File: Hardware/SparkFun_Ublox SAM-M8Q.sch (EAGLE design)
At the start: 34 parts, among them J13 Qwiic Right Angle, J4 Qwiic Right Angle, U2 UBLOX_SAM_M8Q-0-10

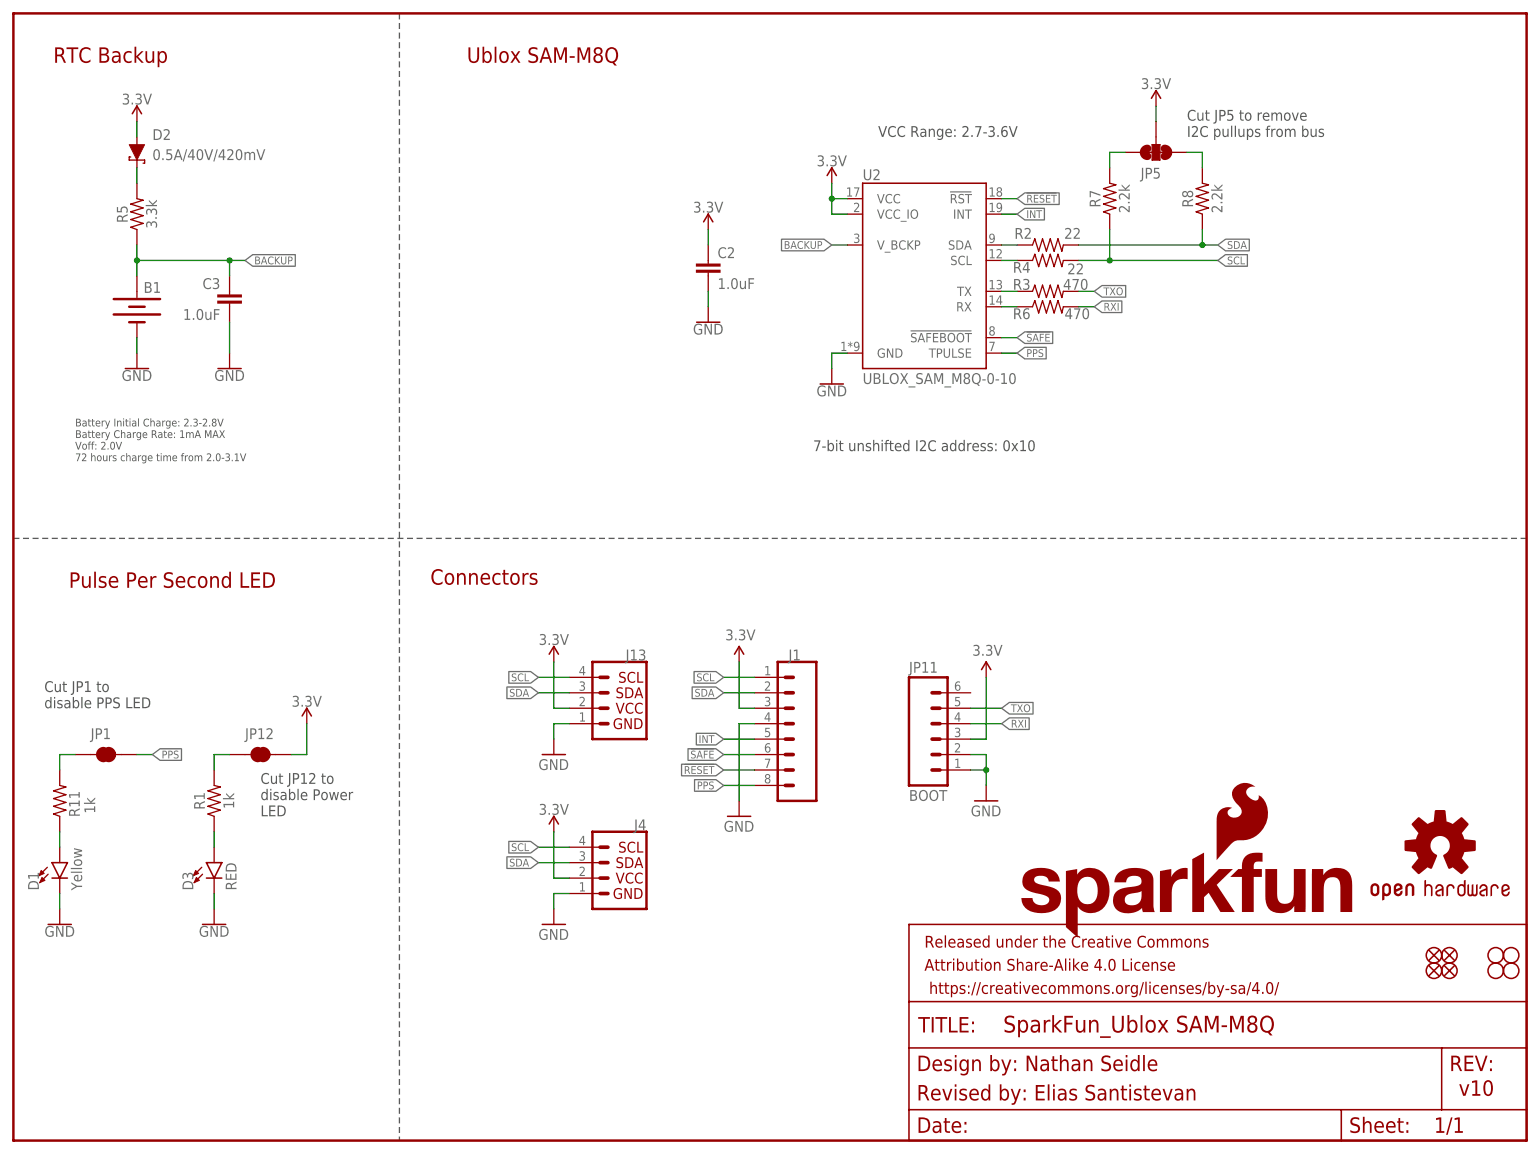
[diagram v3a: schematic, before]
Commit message: Changes JP12 to JP2, fixes SDA trace, adds silk on top
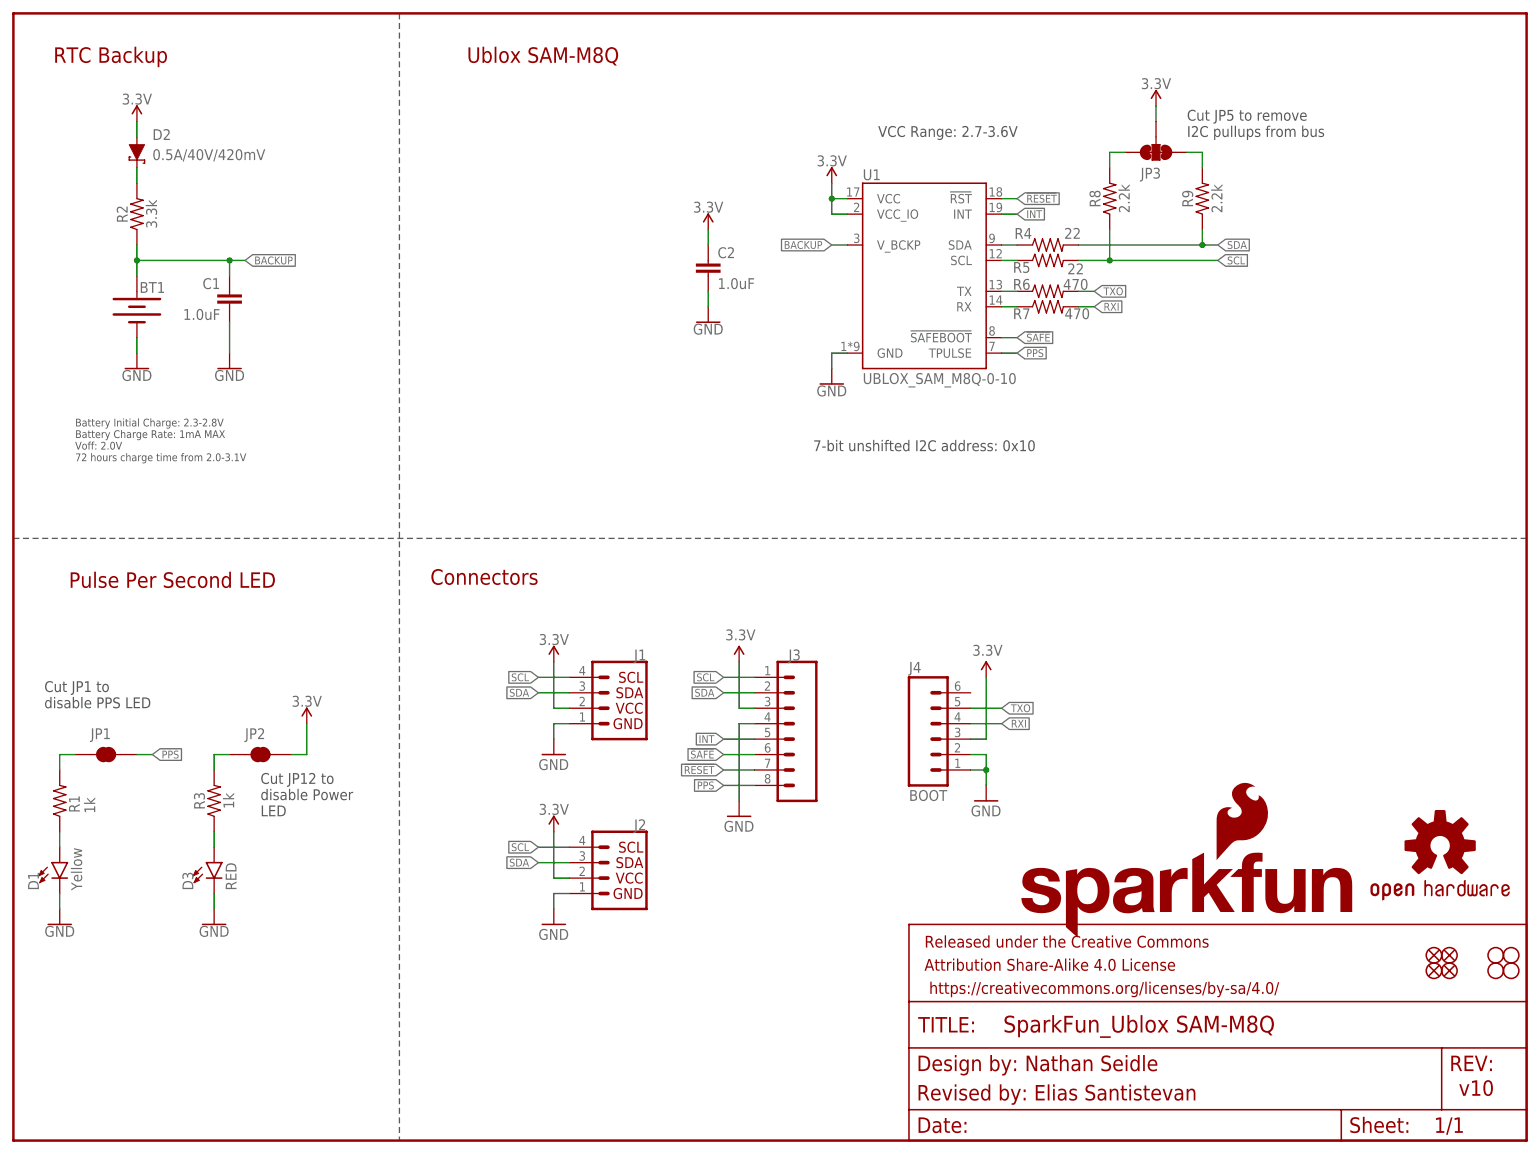
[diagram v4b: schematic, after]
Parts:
- removed J13: Qwiic Right Angle, SparkFun-Connectors:I2C_STANDARDQWIIC
- removed JP11: BOOT, SparkFun-Connectors:CONN_06NO_SILK_NO_POP
- removed JP12: JUMPER-SMT_2_NC_TRACE_SILK, SparkFun-Jumpers:JUMPER-SMT_2_NC_TRACE_SILK
- removed JP5: JUMPER-SMT_3_2-NC_TRACE_SILK, SparkFun-Jumpers:JUMPER-SMT_3_2-NC_TRACE_SILK
- removed R11: 1k, SparkFun-Resistors:1KOHM-0603-1/10W-1%
- added FD1: FIDUCIALUFIDUCIAL, SparkFun-Aesthetics:FIDUCIALUFIDUCIAL
- added H3: STAND-OFF, SparkFun-Hardware:STAND-OFF
- added J2: Qwiic Right Angle, SparkFun-Connectors:I2C_STANDARDQWIIC
- added J3: (no value), SparkFun-Connectors:CONN_08NO_SILK_FEMALE_PTH
- added R9: 2.2k, SparkFun-Resistors:2.2KOHM-0603-1/10W-1%
- J1: value (none) -> Qwiic Right Angle; device SparkFun-Connectors:CONN_08NO_SILK_FEMALE_PTH -> SparkFun-Connectors:I2C_STANDARDQWIIC
- J4: value Qwiic Right Angle -> BOOT; device SparkFun-Connectors:I2C_STANDARDQWIIC -> SparkFun-Connectors:CONN_06NO_SILK_NO_POP
- JP2: value FIDUCIALUFIDUCIAL -> JUMPER-SMT_2_NC_TRACE_SILK; device SparkFun-Aesthetics:FIDUCIALUFIDUCIAL -> SparkFun-Jumpers:JUMPER-SMT_2_NC_TRACE_SILK
- JP3: value STAND-OFF -> JUMPER-SMT_3_2-NC_TRACE_SILK; device SparkFun-Hardware:STAND-OFF -> SparkFun-Jumpers:JUMPER-SMT_3_2-NC_TRACE_SILK
- LOGO1: value OSHW-LOGOMINI -> SFE_LOGO_NAME_FLAME.2_INCH; device SparkFun-Aesthetics:OSHW-LOGOMINI -> SparkFun-Aesthetics:SFE_LOGO_NAME_FLAME.2_INCH
- LOGO2: value SFE_LOGO_NAME_FLAME.2_INCH -> OSHW-LOGOM; device SparkFun-Aesthetics:SFE_LOGO_NAME_FLAME.2_INCH -> SparkFun-Aesthetics:OSHW-LOGOM
- R2: value 22 -> 3.3k; device SparkFun-Resistors:22OHM-0603-1/10W-1% -> SparkFun-Resistors:3.3KOHM-0603-1/10W-1%
- R3: value 470 -> 1k; device SparkFun-Resistors:470OHM-0603-1/10W-1% -> SparkFun-Resistors:1KOHM-0603-1/10W-1%
- R5: value 3.3k -> 22; device SparkFun-Resistors:3.3KOHM-0603-1/10W-1% -> SparkFun-Resistors:22OHM-0603-1/10W-1%
- R7: value 2.2k -> 470; device SparkFun-Resistors:2.2KOHM-0603-1/10W-1% -> SparkFun-Resistors:470OHM-0603-1/10W-1%
- renumbered B1 to BT1, C3 to C1, JP10 to H2, JP4 to H4, JP6 to FD3, JP7 to FD2, JP8 to FD4, JP9 to H1, U2 to U1
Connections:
- net !RESET: now also J3.7; no longer J1.7
- net !SAFE: now also J3.6; no longer J1.6
- net 3.3V: now also J1.2, J2.2, J3.3, J4.3, JP2.2, JP3.2; no longer J1.3, J13.2, J4.2, JP11.3, JP12.2, JP5.2
- net BACKUP: now also R2.1; no longer R5.1
- net GND: now also J1.1, J2.1, J3.4, J4.2; no longer J1.4, J13.1, JP11.1, JP11.2
- net INT: now also J3.5; no longer J1.5
- net N$1: now also JP2.1, R3.2; no longer JP12.1, R1.2
- net N$2: now also R1.1; no longer R11.1
- net N$3: now also R3.1; no longer R1.1
- net N$4: now also R1.2; no longer R11.2
- net N$5: now also JP3.1, R9.2; no longer JP5.1, R8.2
- net N$6: now also R2.2; no longer R5.2
- net N$8: now also JP3.3, R8.2; no longer JP5.3, R7.2
- net PPS: now also J3.8; no longer J1.8
- net RXI: now also J4.4, R7.2; no longer JP11.4, R6.2
- net RXLV: now also R7.1; no longer R6.1
- net SCL: now also J1.4, J2.4, J3.1, R5.2, R8.1; no longer J1.1, J13.4, J4.4, R4.2, R7.1
- net SCL_LV: now also R5.1; no longer R4.1
- net SDA: now also J1.3, J2.3, J3.2, R4.2, R9.1; no longer J1.2, J13.3, J4.3, R2.2, R8.1
- net SDA_LV: now also R4.1; no longer R2.1
- net TXLV: now also R6.1; no longer R3.1
- net TXO: now also J4.5, R6.2; no longer JP11.5, R3.2
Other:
- moved on the sheet: R1, R2, R3, R4, R5, R6, R7, R8

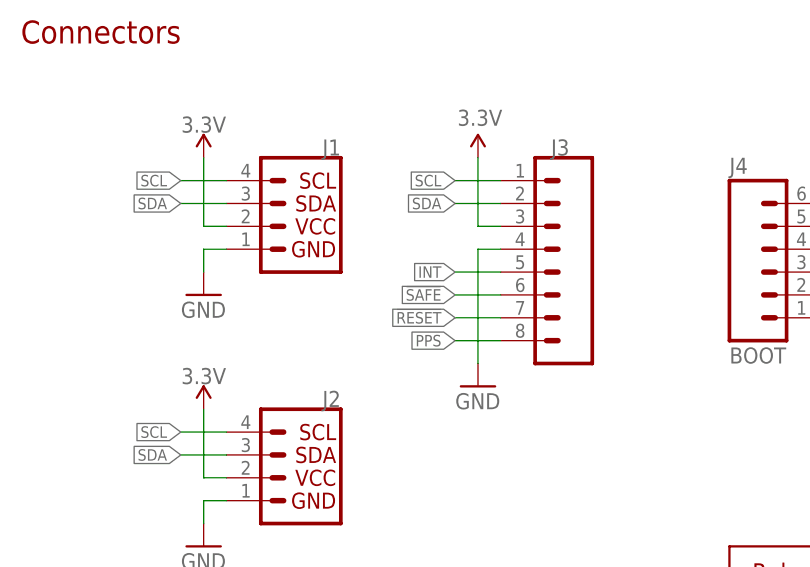
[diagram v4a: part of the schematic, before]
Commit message: Changes polygon width to 10 mil and dimension to 8 mil
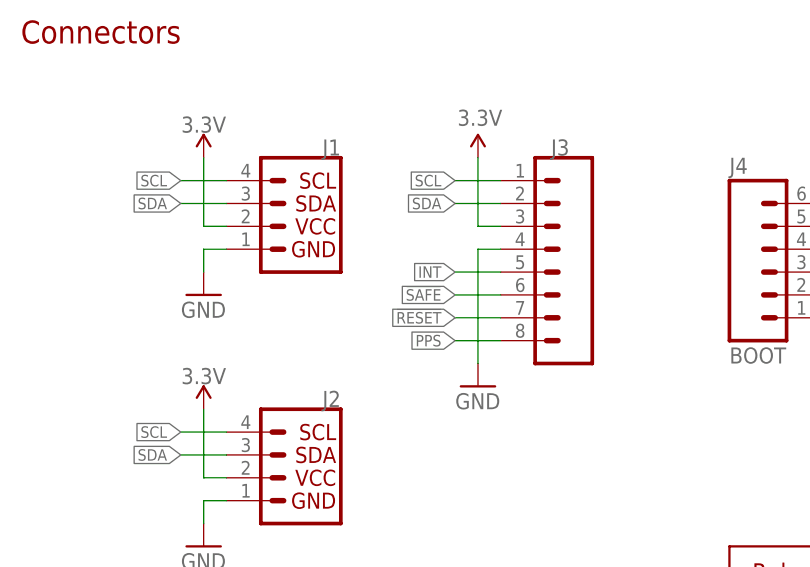
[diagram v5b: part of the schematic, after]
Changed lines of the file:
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@@
 <pinref part="J3" gate="G$1" pin="5"/>
 <wire x1="121.92" y1="66.04" x2="116.84" y2="66.04" width="0.1524" layer="91"/>
-<label x="116.84" y="66.04" size="1.27" layer="95" font="vector" ratio="12" rot="R180" xref="yes"/>
+<label x="116.84" y="66.04" size="1.27" layer="95" font="vector" rot="R180" xref="yes"/>
 </segment>
 </net>
@@
 <pinref part="J3" gate="G$1" pin="6"/>
 <wire x1="121.92" y1="63.5" x2="116.84" y2="63.5" width="0.1524" layer="91"/>
-<label x="116.84" y="63.5" size="1.27" layer="95" font="vector" ratio="12" rot="R180" xref="yes"/>
+<label x="116.84" y="63.5" size="1.27" layer="95" font="vector" rot="R180" xref="yes"/>
 </segment>
 </net>

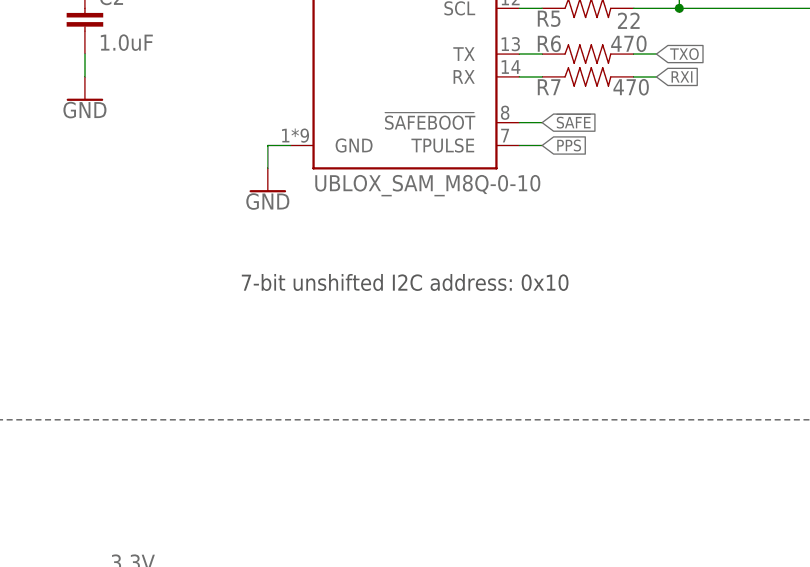
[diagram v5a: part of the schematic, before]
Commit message: Updates address to correct default and only: 0x42
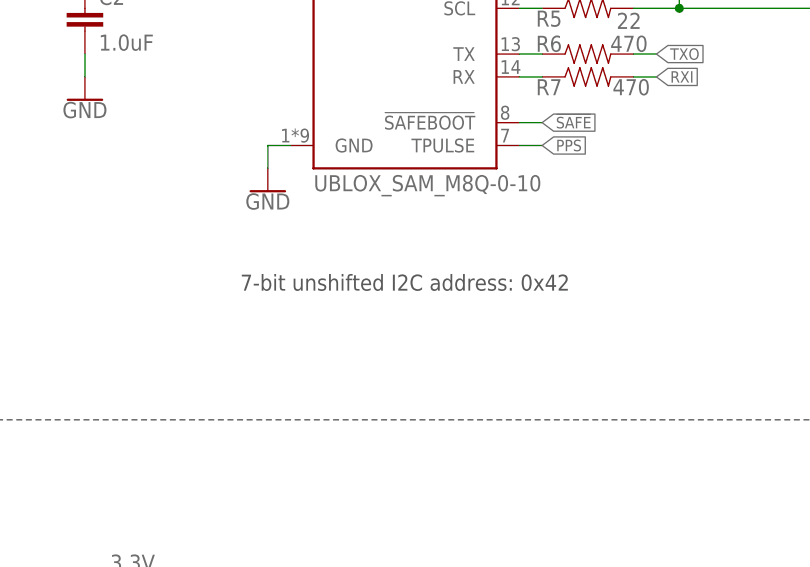
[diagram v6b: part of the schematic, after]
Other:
- note added: "7-bit unshifted I2C address: 0x42"
- note removed: "7-bit unshifted I2C address: 0x10"
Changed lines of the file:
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@@
 <plain>
 <text x="237.744" y="7.366" size="2.54" layer="94" font="vector">v10</text>
-<text x="149.86" y="114.3" size="1.778" layer="97" font="vector" align="center">7-bit unshifted I2C address: 0x10</text>
+<text x="149.86" y="114.3" size="1.778" layer="97" font="vector" align="center">7-bit unshifted I2C address: 0x42</text>
 <text x="87.122" y="178.562" size="2.54" layer="94" font="vector" ratio="12" rot="MR180" align="center">Ublox SAM-M8Q</text>
 <text x="16.002" y="178.562" size="2.54" layer="94" font="vector" ratio="12" rot="MR180" align="center">RTC Backup</text>
